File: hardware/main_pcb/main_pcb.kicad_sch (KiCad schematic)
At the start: 51 parts

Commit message: Added component footprints
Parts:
- added C14: 100nF, Capacitor_SMD:C_0603_1608Metric, symbol Device:C
- added H1: MountingHole, Knob:holes, symbol Mechanical:MountingHole
- added J6: PROG, Connector_PinHeader_2.54mm:PinHeader_1x03_P2.54mm_Vertical, symbol Connector_Generic:Conn_01x03
- added R15, R16: 10k, Resistor_SMD:R_0603_1608Metric, symbol Device:R
- added TP1: EN, TestPoint:TestPoint_Pad_D2.0mm, symbol Connector:TestPoint
- added TP2: GP0, TestPoint:TestPoint_Pad_D2.0mm, symbol Connector:TestPoint
- C1, C10, C12, C2, C9: renamed from C?; footprint (none) -> Capacitor_SMD:C_0603_1608Metric
- C11, C13, C3, C4, C5, C6, C7, C8: renamed from C?; footprint (none) -> Capacitor_SMD:C_0805_2012Metric
- C15: renamed from C?; value C -> 100nF; footprint (none) -> Capacitor_SMD:C_0603_1608Metric
- J1: renamed from J?; footprint (none) -> Connector_USB:USB_C_Receptacle_HRO_TYPE-C-31-M-12; LCSC (none) -> C165948
- J2: renamed from J?; footprint (none) -> Connector_JST:JST_XH_B2B-XH-AM_1x02_P2.50mm_Vertical
- J4: renamed from J?; footprint (none) -> Connector_Hirose:Hirose_DF52-12S-0.8H_1x12-1MP_P0.80mm_Horizontal
- J5: renamed from J?; footprint (none) -> Connector_Hirose:Hirose_DF52-8S-0.8H_1x08-1MP_P0.80mm_Horizontal
- L1: renamed from L?; footprint (none) -> Sunlord:MWSA0402S-6R8MT; LCSC (none) -> C408332; MFN (none) -> MWSA0402S-1R0MT
- L2: renamed from L?; footprint (none) -> Sunlord:MWSA0402S-6R8MT; LCSC (none) -> C408338
- R1, R10, R11, R12, R13, R14, R2, R3, R4, R5, R7, R8, R9: renamed from R?; footprint (none) -> Resistor_SMD:R_0603_1608Metric
- R6: renamed from R?; value R -> 4.7k; footprint (none) -> Resistor_SMD:R_0603_1608Metric
- SW1: renamed from SW?; footprint (none) -> Yuandi:TS-1068A-A2B3-D2; LCSC (none) -> C498297
- U1: renamed from U?; footprint (none) -> Package_SO:SOP-8-1EP_4.57x4.57mm_P1.27mm_EP4.57x4.45mm_ThermalVias
- gave numbers to parts that had none: 15
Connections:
- net +3.3V: now also R15.1, R16.1
- net GND: now also Q1.2 (S), C14.2, J6.3 (Pin_3)
- net at U4.27 (GPIO0/BOOT): now also R16.2, TP2.1
- net at U4.3 (EN): now also C14.1, R15.2, TP1.1
- net at U4.36 (U0RXD/GPIO44/CLK_OUT2): now also J6.2 (Pin_2)
- net at U4.37 (U0TXD/GPIO43/CLK_OUT1): now also J6.1 (Pin_1)
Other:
- moved on the sheet: C1, C10, C11, C12, C13, C15, C2, C3, C4, C5, C6, C7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

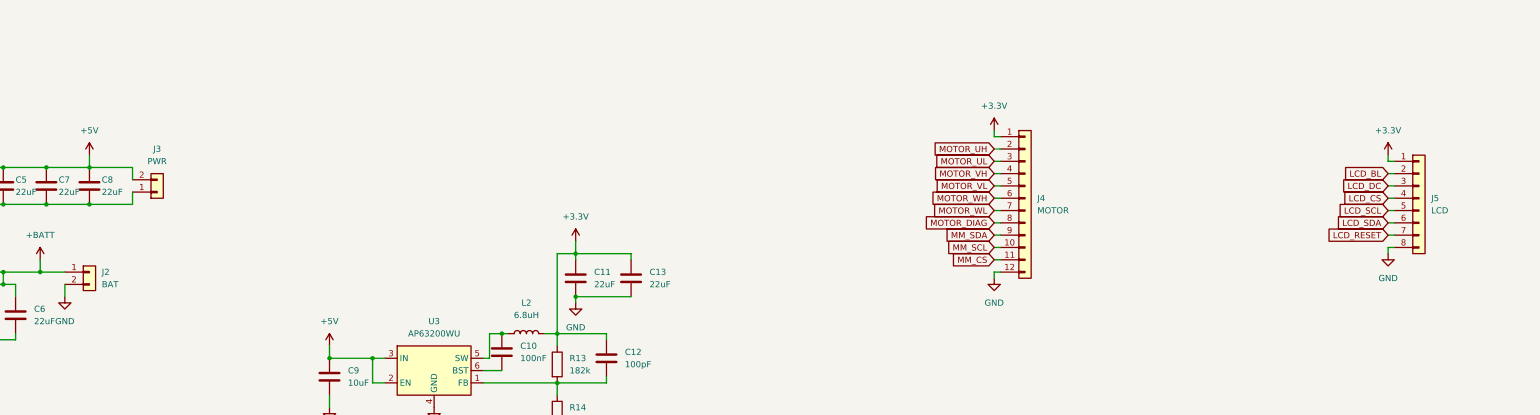
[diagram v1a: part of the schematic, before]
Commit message: Updated connectors
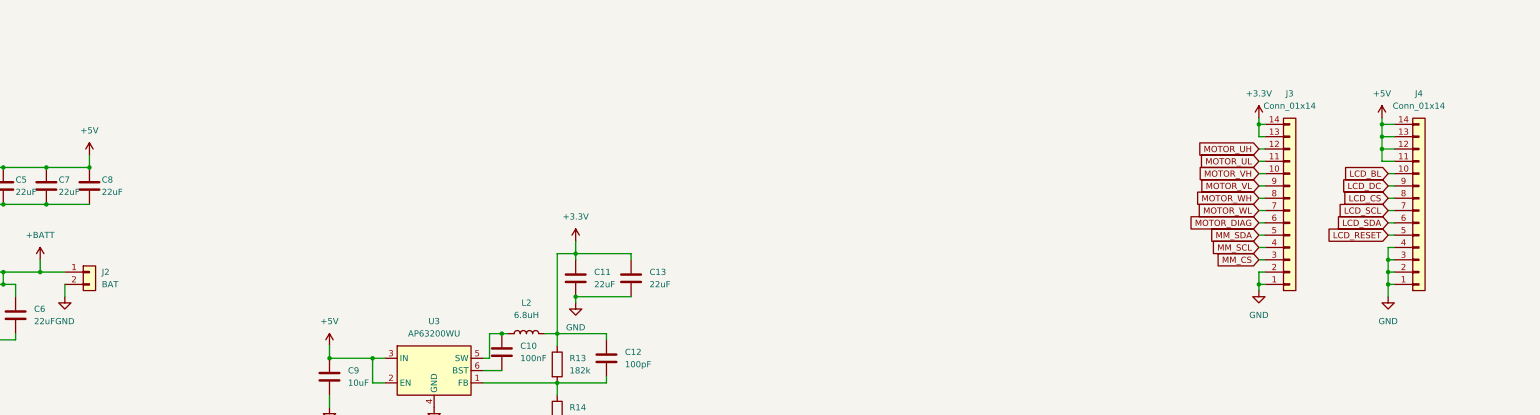
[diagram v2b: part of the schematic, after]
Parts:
- removed J3: PWR, Connector_PinSocket_2.54mm:PinSocket_1x02_P2.54mm_Vertical, symbol Connector_Generic:Conn_01x02
- removed J4: MOTOR, Connector_Hirose:Hirose_DF52-12S-0.8H_1x12-1MP_P0.80mm_Horizontal, symbol Connector_Generic:Conn_01x12
- removed J5: LCD, Connector_Hirose:Hirose_DF52-8S-0.8H_1x08-1MP_P0.80mm_Horizontal, symbol Connector_Generic:Conn_01x08
- added J3, J4: Conn_01x14, Jushuo:FPC_14, symbol Connector_Generic:Conn_01x14
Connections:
- net +3.3V: now also J3.13 (Pin_13), J3.14 (Pin_14)
- net +5V: now also J4.11 (Pin_11), J4.12 (Pin_12), J4.13 (Pin_13), J4.14 (Pin_14)
- net GND: now also J3.1 (Pin_1), J3.2 (Pin_2), J4.1 (Pin_1), J4.2 (Pin_2), J4.3 (Pin_3), J4.4 (Pin_4)
- net LCD_BL: now also J4.10 (Pin_10)
- net LCD_CS: now also J4.8 (Pin_8)
- net LCD_DC: now also J4.9 (Pin_9)
- net LCD_RESET: now also J4.5 (Pin_5)
- net LCD_SCL: now also J4.7 (Pin_7)
- net LCD_SDA: now also J4.6 (Pin_6)
- net MM_CS: now also J3.3 (Pin_3)
- net MM_SCL: now also J3.4 (Pin_4)
- net MM_SDA: now also J3.5 (Pin_5)
- net MOTOR_DIAG: now also J3.6 (Pin_6)
- net MOTOR_UH: now also J3.12 (Pin_12)
- net MOTOR_UL: now also J3.11 (Pin_11)
- net MOTOR_VH: now also J3.10 (Pin_10)
- net MOTOR_VL: now also J3.9 (Pin_9)
- net MOTOR_WH: now also J3.8 (Pin_8)
- net MOTOR_WL: now also J3.7 (Pin_7)

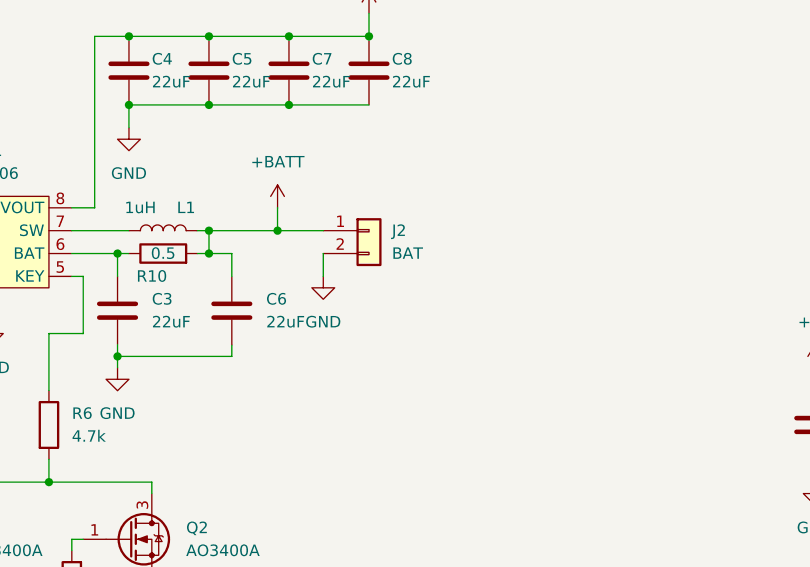
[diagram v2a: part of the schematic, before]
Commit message: Updated battery connector
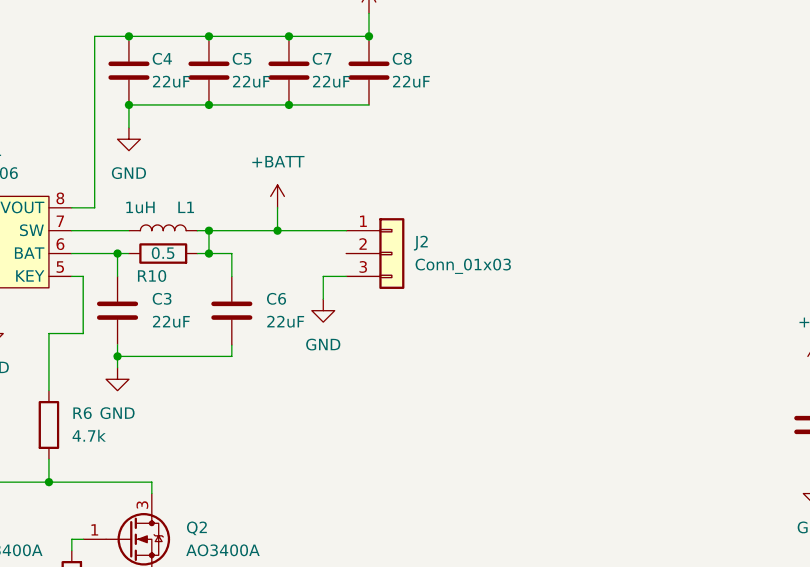
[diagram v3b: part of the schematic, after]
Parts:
- removed J2: BAT, Connector_JST:JST_XH_B2B-XH-AM_1x02_P2.50mm_Vertical, symbol Connector_Generic:Conn_01x02
- added J2: Conn_01x03, Connector_Molex:Molex_PicoBlade_53261-0371_1x03-1MP_P1.25mm_Horizontal, symbol Connector_Generic:Conn_01x03
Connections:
- net +BATT: now also J2.1 (Pin_1)
- net GND: now also J2.3 (Pin_3)
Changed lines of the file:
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@@
     (stroke (width 0) (type default) (color 0 0 0 0))
   )
-  (wire (pts (xy 87.63 227.33) (xy 92.71 227.33))
+  (wire (pts (xy 87.63 227.33) (xy 95.25 227.33))
     (stroke (width 0) (type default) (color 0 0 0 0))
   )
@@
     (stroke (width 0) (type default) (color 0 0 0 0))
   )
-  (wire (pts (xy 92.71 229.87) (xy 92.71 232.41))
+  (wire (pts (xy 92.71 232.41) (xy 92.71 234.95))
     (stroke (width 0) (type default) (color 0 0 0 0))
   )
@@
   )
   (wire (pts (xy 64.77 224.79) (xy 67.31 224.79))
+    (stroke (width 0) (type default) (color 0 0 0 0))
+  )
+  (wire (pts (xy 92.71 232.41) (xy 95.25 232.41))
     (stroke (width 0) (type default) (color 0 0 0 0))
   )
@@
     (pin "1")
   )
+  (symbol (lib_id "Connector_Generic:Conn_01x03") (at 100.33 229.87 0) (unit 1)
+    (in_bom yes) (on_board yes) (fields_autoplaced)
+    (property "Reference" "J2" (id 0) (at 102.87 228.5999 0)
+      (effects (font (size 1.27 1.27)) (justify left))
+    )
+    (property "Value" "Conn_01x03" (id 1) (at 102.87 231.1399 0)
+      (effects (font (size 1.27 1.27)) (justify left))
+    )
+    (property "Footprint" "Connector_Molex:Molex_PicoBlade_53261-0371_1x03-1MP_P1.25mm_Horizontal" (id 2) (at 100.33 229.87 0)
+      (effects (font (size 1.27 1.27)) hide)
+    )
+    (property "Datasheet" "~" (id 3) (at 100.33 229.87 0)
+      (effects (font (size 1.27 1.27)) hide)
+    )
+    (pin "1")
+    (pin "2")
+    (pin "3")
+  )
   (symbol (lib_id "power:VBUS") (at 30.48 222.25 0) (unit 1)
     (in_bom yes) (on_board yes) (fields_autoplaced)
@@
     )
     (property "LCSC" "C498297" (id 4) (at 27.94 119.38 90)
-      (effects (font (size 1.27 1.27)) hide)
-    )
-    (pin "1")
-    (pin "2")
-  )
-  (symbol (lib_id "Connector_Generic:Conn_01x02") (at 97.79 227.33 0) (unit 1)
-    (in_bom yes) (on_board yes) (fields_autoplaced)
-    (property "Reference" "J2" (id 0) (at 100.33 227.3299 0)
-      (effects (font (size 1.27 1.27)) (justify left))
-    )
-    (property "Value" "BAT" (id 1) (at 100.33 229.8699 0)
-      (effects (font (size 1.27 1.27)) (justify left))
-    )
-    (property "Footprint" "Connector_JST:JST_XH_B2B-XH-AM_1x02_P2.50mm_Vertical" (id 2) (at 97.79 227.33 0)
-      (effects (font (size 1.27 1.27)) hide)
-    )
-    (property "Datasheet" "~" (id 3) (at 97.79 227.33 0)
       (effects (font (size 1.27 1.27)) hide)
     )
@@
     (pin "2")
   )
-  (symbol (lib_id "power:GND") (at 92.71 232.41 0) (unit 1)
-    (in_bom yes) (on_board yes) (fields_autoplaced)
-    (property "Reference" "#PWR014" (id 0) (at 92.71 238.76 0)
-      (effects (font (size 1.27 1.27)) hide)
-    )
-    (property "Value" "GND" (id 1) (at 92.71 237.49 0))
-    (property "Footprint" "" (id 2) (at 92.71 232.41 0)
-      (effects (font (size 1.27 1.27)) hide)
-    )
-    (property "Datasheet" "" (id 3) (at 92.71 232.41 0)
+  (symbol (lib_id "power:GND") (at 92.71 234.95 0) (unit 1)
+    (in_bom yes) (on_board yes) (fields_autoplaced)
+    (property "Reference" "#PWR014" (id 0) (at 92.71 241.3 0)
+      (effects (font (size 1.27 1.27)) hide)
+    )
+    (property "Value" "GND" (id 1) (at 92.71 240.03 0))
+    (property "Footprint" "" (id 2) (at 92.71 234.95 0)
+      (effects (font (size 1.27 1.27)) hide)
+    )
+    (property "Datasheet" "" (id 3) (at 92.71 234.95 0)
       (effects (font (size 1.27 1.27)) hide)
     )
@@
       (reference "J1") (unit 1) (value "USB_C_Receptacle_USB2.0") (footprint "Connector_USB:USB_C_Receptacle_HRO_TYPE-C-31-M-12")
     )
-    (path "/3a55e2c0-bcf6-46f5-b212-64ef5f5da8a5"
-      (reference "J2") (unit 1) (value "BAT") (footprint "Connector_JST:JST_XH_B2B-XH-AM_1x02_P2.50mm_Vertical")
+    (path "/2c85f701-e987-41d7-bc52-485aa4f208b1"
+      (reference "J2") (unit 1) (value "Conn_01x03") (footprint "Connector_Molex:Molex_PicoBlade_53261-0371_1x03-1MP_P1.25mm_Horizontal")
     )
     (path "/e86aca84-1568-46b3-8c95-919273e5ae11"

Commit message: Finished routing
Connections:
- net BAT_ADC: now also U4.5 (GPIO5/TOUCH5/ADC1_CH4)
- net BAT_ADC_EN: now also U4.6 (GPIO6/TOUCH6/ADC1_CH5)
- net IO_OFF: now also U4.15 (GPIO3/TOUCH3/ADC1_CH2)
- net LCD_BL: now also U4.32 (MTCK/GPIO39/CLK_OUT3/SUBSPICS1)
- net LCD_CS: now also U4.34 (MTDI/GPIO41/CLK_OUT1)
- net LCD_DC: now also U4.33 (MTDO/GPIO40/CLK_OUT2)
- net LCD_RESET: now also U4.39 (GPIO1/TOUCH1/ADC1_CH0)
- net LCD_SCL: now also U4.35 (MTMS/GPIO42)
- net LCD_SDA: now also U4.38 (GPIO2/TOUCH2/ADC1_CH1)
- net MM_CS: now also U4.31 (GPIO38/FSPIWP/SUBSPIWP)
- net MM_SCL: now also U4.30 (SPIDQS/GPIO37/FSPIQ/SUBSPIQ)
- net MM_SDA: now also U4.29 (SPIIO7/GPIO36/FSPICLK/SUBSPICLK)
- net MOTOR_DIAG: now also U4.28 (SPIIO6/GPIO35/FSPID/SUBSPID)
- net MOTOR_UH: now also U4.20 (GPIO12/TOUCH12/ADC2_CH1/FSPICLK/FSPIIO6/SUBSPICLK)
- net MOTOR_UL: now also U4.21 (GPIO13/TOUCH13/ADC2_CH2/FSPIQ/FSPIIO7/SUBSPIQ)
- net MOTOR_VH: now also U4.22 (GPIO14/TOUCH14/ADC2_CH3/FSPIWP/FSPIDQS/SUBSPIWP)
- net MOTOR_VL: now also U4.23 (GPIO21)
- net MOTOR_WH: now also U4.24 (GPIO47/SPICLK_P/SUBSPICLK_P_DIFF)
- net MOTOR_WL: now also U4.25 (GPIO48/SPICLK_N/SUBSPICLK_N_DIFF)
- net PUSH: now also U4.18 (GPIO10/TOUCH10/ADC1_CH9/FSPICS0/FSPIIO4/SUBSPICS0)
- net PUSH_UP: now also U4.17 (GPIO9/TOUCH9/ADC1_CH8/FSPIHD/SUBSPIHD)
- net RGB: now also U4.4 (GPIO4/TOUCH4/ADC1_CH3)
- no-connect marks 3 -> 5
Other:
- moved on the sheet: C14
